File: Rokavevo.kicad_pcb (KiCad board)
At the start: 2 copper layers, 44 parts, among them J1 AudioJack2_Ground_Switch, Q1 BC847, Q2 BC847, Q3 BC847, Q4 BC847, Q5 BC847, SW1 SW_Nidec_CAS-120A1, U1 LM358, Y1 3579kHz

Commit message: Add files via upload
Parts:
- moved L1 2.82 mm to (105.4, 99.3), turned to 180 degrees
- moved C3 1.99 mm to (108.3, 97.7), turned to 90 degrees
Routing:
- net /RF BPF: track 30.3 -> 24.4 mm
- net /ANT: track 10.8 -> 13.6 mm
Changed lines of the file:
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@@
 	(footprint "Capacitor_SMD:C_0805_2012Metric_Pad1.18x1.45mm_HandSolder"
 		(layer "F.Cu")
-		(at 110.2 98.3375 -90)
+		(at 108.3 97.7375 90)
 		(descr "Capacitor SMD 0805 (2012 Metric), square (rectangular) end terminal, IPC-7351 nominal with elongated pad for handsoldering. (Body size source: IPC-SM-782 page 76, https://www.pcb-3d.com/wordpress/wp-content/uploads/ipc-sm-782a_amendment_1_and_2.pdf, https://docs.google.com/spreadsheets/d/1BsfQQcO9C6DZCsRaXUlFlo91Tg2WpOkGARC1WS5S8t0/edit?usp=sharing), generated with kicad-footprint-generator")
 		(tags "capacitor handsolder")
@@
 		(attr smd)
 		(fp_line
-			(start -0.261252 0.735)
-			(end 0.261252 0.735)
+			(start -0.261252 -0.735)
+			(end 0.261252 -0.735)
 			(stroke
 				(width 0.12)
@@
 		)
 		(fp_line
-			(start -0.261252 -0.735)
-			(end 0.261252 -0.735)
+			(start -0.261252 0.735)
+			(end 0.261252 0.735)
 			(stroke
 				(width 0.12)
@@
 		)
 		(fp_line
-			(start -1.88 0.98)
-			(end -1.88 -0.98)
+			(start 1.88 -0.98)
+			(end 1.88 0.98)
 			(stroke
 				(width 0.05)
@@
 		)
 		(fp_line
-			(start 1.88 0.98)
-			(end -1.88 0.98)
+			(start -1.88 -0.98)
+			(end 1.88 -0.98)
 			(stroke
 				(width 0.05)
@@
 		)
 		(fp_line
-			(start -1.88 -0.98)
-			(end 1.88 -0.98)
+			(start 1.88 0.98)
+			(end -1.88 0.98)
 			(stroke
 				(width 0.05)
@@
 		)
 		(fp_line
-			(start 1.88 -0.98)
-			(end 1.88 0.98)
+			(start -1.88 0.98)
+			(end -1.88 -0.98)
 			(stroke
 				(width 0.05)
@@
 		)
 		(fp_line
-			(start -1 0.625)
-			(end -1 -0.625)
+			(start 1 -0.625)
+			(end 1 0.625)
 			(stroke
 				(width 0.1)
@@
 		)
 		(fp_line
-			(start 1 0.625)
-			(end -1 0.625)
+			(start -1 -0.625)
+			(end 1 -0.625)
 			(stroke
 				(width 0.1)
@@
 		)
 		(fp_line
-			(start -1 -0.625)
-			(end 1 -0.625)
+			(start 1 0.625)
+			(end -1 0.625)
 			(stroke
 				(width 0.1)
@@
 		)
 		(fp_line
-			(start 1 -0.625)
-			(end 1 0.625)
+			(start -1 0.625)
+			(end -1 -0.625)
 			(stroke
 				(width 0.1)
@@
 		)
 		(pad "1" smd roundrect
-			(at -1.0375 0 270)
+			(at -1.0375 0 90)
 			(size 1.175 1.45)
 			(layers "F.Cu" "F.Mask" "F.Paste")
@@
 		)
 		(pad "2" smd roundrect
-			(at 1.0375 0 270)
+			(at 1.0375 0 90)
 			(size 1.175 1.45)
 			(layers "F.Cu" "F.Mask" "F.Paste")
@@
 	(footprint "Connector_PinHeader_2.54mm:PinHeader_1x02_P2.54mm_Vertical"
 		(layer "F.Cu")
-		(at 107.2 97.1)
+		(at 105.4 99.275 180)
 		(descr "Through hole straight pin header, 1x02, 2.54mm pitch, single row")
 		(tags "Through hole pin header THT 1x02 2.54mm single row")
@@
 		(attr through_hole)
 		(fp_line
-			(start -1.38 -1.38)
-			(end 0 -1.38)
+			(start 1.38 1.27)
+			(end 1.38 3.92)
 			(stroke
 				(width 0.12)
@@
 		)
 		(fp_line
-			(start -1.38 0)
-			(end -1.38 -1.38)
+			(start -1.38 3.92)
+			(end 1.38 3.92)
 			(stroke
 				(width 0.12)
@@
 		(fp_line
 			(start -1.38 1.27)
-			(end -1.38 3.92)
+			(end 1.38 1.27)
 			(stroke
 				(width 0.12)
@@
 		(fp_line
 			(start -1.38 1.27)
-			(end 1.38 1.27)
+			(end -1.38 3.92)
 			(stroke
 				(width 0.12)
@@
 		)
 		(fp_line
-			(start -1.38 3.92)
-			(end 1.38 3.92)
+			(start -1.38 0)
+			(end -1.38 -1.38)
 			(stroke
 				(width 0.12)
@@
 		)
 		(fp_line
-			(start 1.38 1.27)
-			(end 1.38 3.92)
+			(start -1.38 -1.38)
+			(end 0 -1.38)
 			(stroke
 				(width 0.12)
@@
 		)
 		(fp_line
-			(start -1.77 -1.77)
-			(end -1.77 4.32)
+			(start 1.77 4.32)
+			(end 1.77 -1.77)
 			(stroke
 				(width 0.05)
@@
 		)
 		(fp_line
-			(start -1.77 4.32)
-			(end 1.77 4.32)
+			(start 1.77 -1.77)
+			(end -1.77 -1.77)
 			(stroke
 				(width 0.05)
@@
 		)
 		(fp_line
-			(start 1.77 -1.77)
-			(end -1.77 -1.77)
+			(start -1.77 4.32)
+			(end 1.77 4.32)
 			(stroke
 				(width 0.05)
@@
 		)
 		(fp_line
-			(start 1.77 4.32)
-			(end 1.77 -1.77)
+			(start -1.77 -1.77)
+			(end -1.77 4.32)
 			(stroke
 				(width 0.05)
@@
 		)
 		(fp_line
-			(start -1.27 -0.635)
-			(end -0.635 -1.27)
+			(start 1.27 3.81)
+			(end -1.27 3.81)
 			(stroke
 				(width 0.1)
@@
 		)
 		(fp_line
-			(start -1.27 3.81)
-			(end -1.27 -0.635)
+			(start 1.27 -1.27)
+			(end 1.27 3.81)
 			(stroke
 				(width 0.1)
@@
 		)
 		(fp_line
-			(start 1.27 -1.27)
-			(end 1.27 3.81)
+			(start -1.27 3.81)
+			(end -1.27 -0.635)
 			(stroke
 				(width 0.1)
@@
 		)
 		(fp_line
-			(start 1.27 3.81)
-			(end -1.27 3.81)
+			(start -1.27 -0.635)
+			(end -0.635 -1.27)
 			(stroke
 				(width 0.1)
@@
 		)
 		(pad "1" thru_hole rect
-			(at 0 0)
+			(at 0 0 180)
 			(size 1.7 1.7)
 			(drill 1)
@@
 		)
 		(pad "2" thru_hole circle
-			(at 0 2.54)
+			(at 0 2.54 180)
 			(size 1.7 1.7)
 			(drill 1)
@@
 	)
 	(segment
-		(start 109.935 99.64)
-		(end 110.2 99.375)
+		(start 119.279 94.447644)
+		(end 119.279 92.952356)
 		(width 0.381)
 		(layer "F.Cu")
@@
 	)
 	(segment
-		(start 117.2 98)
-		(end 117.2 96.526644)
-		(width 0.381)
+		(start 108.265 96.735)
+		(end 108.3 96.7)
+		(width 0.2)
 		(layer "F.Cu")
 		(net 3)
 	)
 	(segment
-		(start 108.1 95.5)
-		(end 106.1 95.5)
+		(start 118.326644 92)
+		(end 109.1 92)
 		(width 0.381)
 		(layer "F.Cu")
@@
 	)
 	(segment
-		(start 105.3 96.3)
-		(end 105.3 97.74)
-		(width 0.381)
+		(start 105.4 96.735)
+		(end 108.265 96.735)
+		(width 0.2)
 		(layer "F.Cu")
 		(net 3)
 	)
 	(segment
-		(start 108.9 94.7)
-		(end 108.1 95.5)
+		(start 109.1 92)
+		(end 108.8 92.3)
 		(width 0.381)
 		(layer "F.Cu")
@@
 	)
 	(segment
-		(start 109.960856 92)
-		(end 108.9 93.060856)
+		(start 117.2 98)
+		(end 117.2 96.526644)
 		(width 0.381)
 		(layer "F.Cu")
@@
 	)
 	(segment
-		(start 119.279 92.952356)
-		(end 118.326644 92)
+		(start 117.2 96.526644)
+		(end 119.279 94.447644)
 		(width 0.381)
 		(layer "F.Cu")
@@
 	)
 	(segment
-		(start 106.1 95.5)
-		(end 105.3 96.3)
+		(start 108.3 95.3)
+		(end 108.3 96.7)
 		(width 0.381)
 		(layer "F.Cu")
@@
 	)
 	(segment
-		(start 107.2 99.64)
-		(end 109.935 99.64)
+		(start 108.8 92.3)
+		(end 108.8 94.8)
 		(width 0.381)
 		(layer "F.Cu")
@@
 	)
 	(segment
-		(start 108.9 93.060856)
-		(end 108.9 94.7)
+		(start 119.279 92.952356)
+		(end 118.326644 92)
 		(width 0.381)
 		(layer "F.Cu")
@@
 	)
 	(segment
-		(start 105.3 97.74)
-		(end 107.2 99.64)
+		(start 108.8 94.8)
+		(end 108.3 95.3)
 		(width 0.381)
 		(layer "F.Cu")
@@
 	)
 	(segment
-		(start 118.326644 92)
-		(end 109.960856 92)
+		(start 110.2375 93.6625)
+		(end 110.2 93.7)
 		(width 0.381)
 		(layer "F.Cu")
-		(net 3)
+		(net 4)
 	)
 	(segment
-		(start 117.2 96.526644)
-		(end 119.279 94.447644)
+		(start 112.26 93.84)
+		(end 112 94.1)
 		(width 0.381)
 		(layer "F.Cu")
-		(net 3)
+		(net 4)
 	)
 	(segment
-		(start 119.279 94.447644)
-		(end 119.279 92.952356)
+		(start 108.3 98.775)
+		(end 105.9 98.775)
 		(width 0.381)
 		(layer "F.Cu")
-		(net 3)
+		(net 4)
 	)
 	(segment
-		(start 110.2375 93.6625)
-		(end 110.2 93.7)
+		(start 112 94.1)
+		(end 112 98)
 		(width 0.381)
 		(layer "F.Cu")
@@
 	)
 	(segment
-		(start 111.1 97.1)
-		(end 107.2 97.1)
+		(start 112.26 93.6625)
+		(end 112.26 93.84)
 		(width 0.381)
 		(layer "F.Cu")
@@
 	)
 	(segment
-		(start 110.2 97.3)
-		(end 110.2 93.7)
+		(start 112 98)
+		(end 111.225 98.775)
 		(width 0.381)
 		(layer "F.Cu")
@@
 	)
 	(segment
-		(start 112 98)
-		(end 111.1 97.1)
+		(start 105.9 98.775)
+		(end 105.4 99.275)
+		(width 0.381)
+		(layer "F.Cu")
+		(net 4)
+	)
+	(segment
+		(start 111.225 98.775)
+		(end 108.3 98.775)
 		(width 0.381)
 		(layer "F.Cu")
@@
 		(polygon
 			(pts
-				(xy 100 73) (xy 163.3 73) (xy 163.404418 129.389582) (xy 100 129) (xy 100 73) (xy 100 73)
+				(xy 100 73) (xy 163.3 73) (xy 163.404418 129.389582) (xy 100 129)
 			)
 		)

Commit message: Add files via upload
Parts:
- moved J1 10.3 mm to (157.2, 86.2)
- moved C13 10.2 mm to (143.3, 82.8)
- moved D3 8.51 mm to (110.5, 123.2)
- moved D4 8.51 mm to (115.5, 123.2)
- moved R8 8.19 mm to (115.5, 116.7), turned to -90 degrees
- moved RV1 6.76 mm to (148.9, 111.4)
- moved R11 5.90 mm to (134.7, 120.2)
- moved C8 5.68 mm to (134.1, 117.0)
- moved Q4 5.24 mm to (121.0, 101.0)
- moved C6 5.03 mm to (128.0, 99.8)
- moved Q5 4.61 mm to (128.7, 105.6)
- moved C11 4.39 mm to (135.0, 103.2)
- moved C9 4.39 mm to (123.5, 113.2)
- moved R10 4.39 mm to (137.5, 94.2)
- moved R12 4.39 mm to (117.7, 109.2)
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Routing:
- net Net-(U1B--): track 9.46 -> 23.5 mm
- net Net-(D5-K): track 68.6 -> 75.9 mm
- net /ANT: track 13.6 -> 19.6 mm
- net /RF BPF: track 24.4 -> 30.4 mm
- net Net-(U1B-+): track 11.3 -> 15.3 mm
- net /LNA: track 6.41 -> 10.4 mm
- net Net-(D2-K): track 4.00 -> 7.04 mm
- net Net-(U1A--): track 6.98 -> 9.77 mm
- net Net-(C12-Pad1): track 8.09 -> 5.54 mm
- net Net-(Q3-E): track 8.02 -> 10.6 mm
- net Net-(Q3-B): track 21.5 -> 19.6 mm
- net Net-(Q2-E): track 10.4 -> 12.3 mm
- net /SBM: track 29.7 -> 31.3 mm

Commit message: Add files via upload
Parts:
- removed J1: AudioJack2_Ground_Switch, Connector_Audio:Jack_3.5mm_CUI_SJ1-3515N_Horizontal
- added J2: AudioJack3_SwitchTR, Connector_Audio:Jack_3.5mm_CUI_SJ1-3515N_Horizontal, B.Cu at (157.3, 87.8)
- BT1, L1, RV1, SW1, Y1: moved to B.Cu
- moved C13 13.9 mm to (148.4, 95.8)
- moved RV1 9.90 mm to (139.0, 111.4)
- moved L1 1.41 mm to (105.0, 99.8), turned to 0 degrees
- turned BT1 to 180 degrees
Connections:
- RV1 pad 1: Net-(U1B-+) -> Net-(C12-Pad1)
- RV1 pad 3: Net-(C12-Pad1) -> Net-(U1B-+)
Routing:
- net Net-(U1B--): track 23.5 -> 8.92 mm
- net Net-(D5-K): track 75.9 -> 77.8 mm
- net /RF BPF: track 30.4 -> 28.9 mm
- net /ANT: track 19.6 -> 18.1 mm
- net Net-(Q2-B): track 37.4 -> 36.4 mm
- net /SBM: track 31.3 -> 32.1 mm
- net Net-(C13-Pad2): track 23.0 -> 23.6 mm
- removed copper zone on B.Cu, net GND

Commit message: Add files via upload
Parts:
- RV1: footprint Connector_PinHeader_2.54mm:PinHeader_1x03_P2.54mm_Vertical -> Potentiometer_THT:Potentiometer_Omeg_PC16BU_Vertical
- moved BT1 48.3 mm to (151.5, 74.5), turned to 90 degrees
- moved J2 42.2 mm to (144.8, 128.1), turned to 90 degrees
- moved D3 41.9 mm to (109.4, 81.3), turned to 90 degrees
- moved D2 39.5 mm to (116.3, 77.8), turned to 0 degrees
- moved C2 37.5 mm to (141.0, 77.2), turned to 0 degrees
- moved D4 37.4 mm to (109.4, 86.3), turned to 90 degrees
- moved SW1 37.4 mm to (150.1, 83.5), turned to 0 degrees
- moved L1 36.7 mm to (132.8, 75.8), turned to -90 degrees
- moved D1 36.1 mm to (121.8, 77.8), turned to 0 degrees
- moved R6 35.1 mm to (126.6, 77.2), turned to 180 degrees
- moved C1 33.6 mm to (141.0, 80.2), turned to 0 degrees
- moved Y1 32.3 mm to (109.5, 93.7), turned to 0 degrees
- moved D5 30.7 mm to (151.6, 95.2), turned to 90 degrees
- moved R7 30.5 mm to (121.0, 82.5), turned to -90 degrees
- moved R8 30.3 mm to (115.9, 86.3), turned to 180 degrees
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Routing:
- net Net-(U1A--): track 9.77 -> 14.1 mm
- net Net-(U1B-+): track 15.3 -> 19.0 mm
- net /LNA: track 10.4 -> 13.8 mm
- net Net-(C12-Pad1): track 5.54 -> 3.04 mm
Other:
- board text added: "Rókavevő 80m Gaben 2025 Prototype I."
- board text removed: "Rókavevő 80m Gaben 2025 Prototipus I."

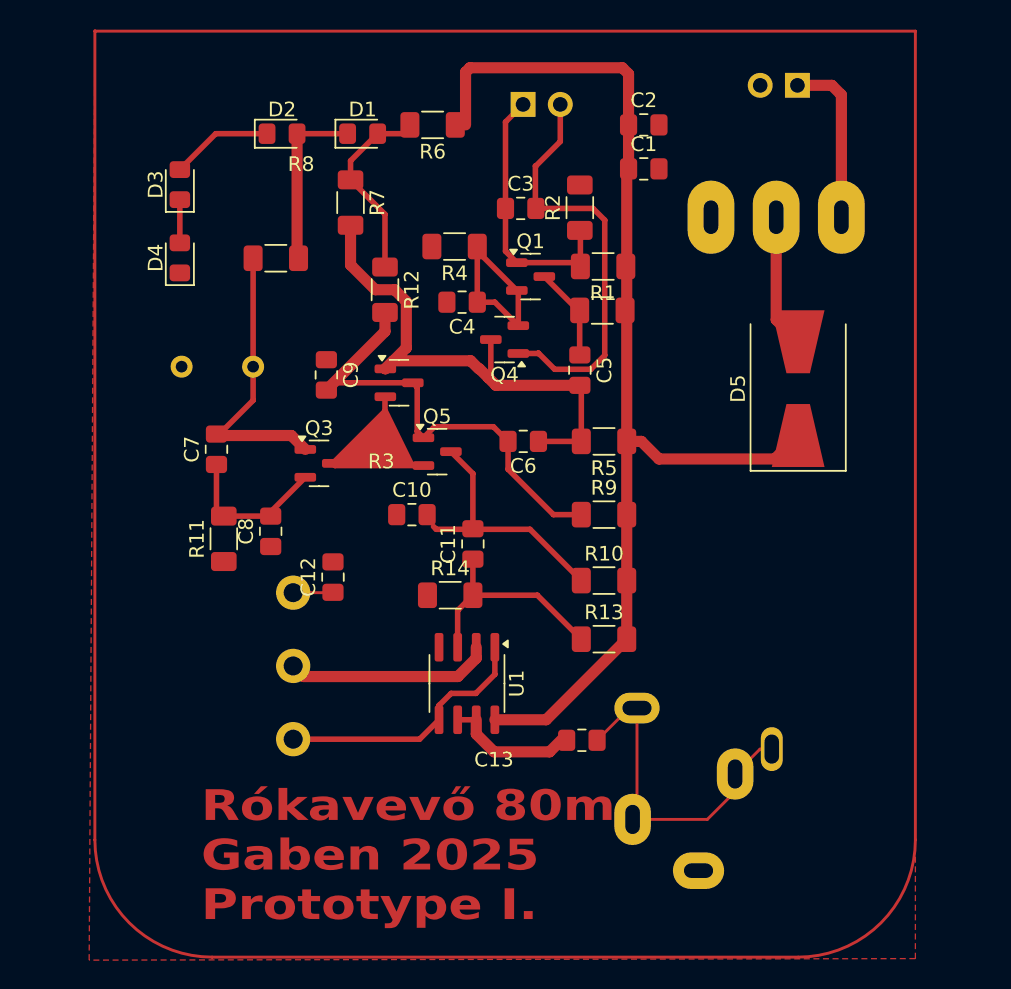
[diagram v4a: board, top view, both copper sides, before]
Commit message: Prototype II
Fixed schematic, new pcb design, Printable mask
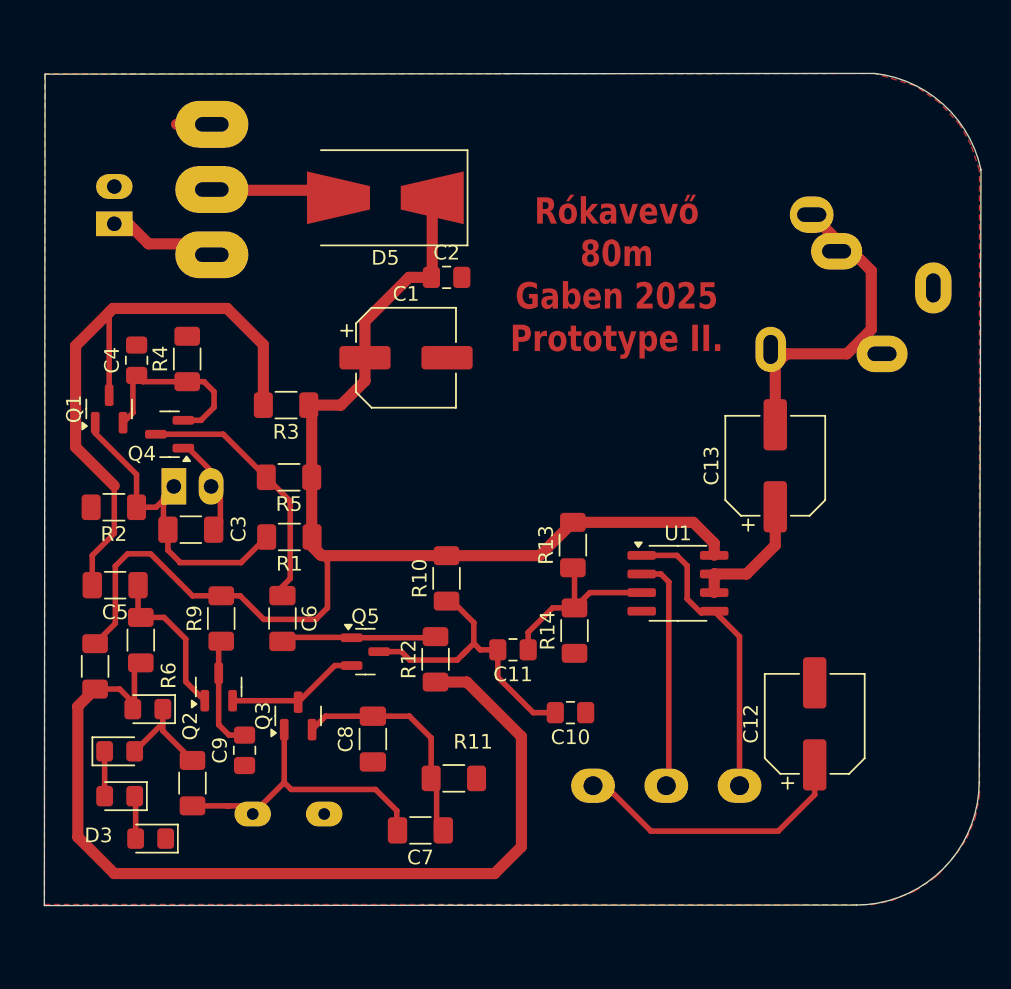
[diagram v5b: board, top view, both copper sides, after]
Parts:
- C1, C12, C13: footprint Capacitor_SMD:C_0805_2012Metric_Pad1.18x1.45mm_HandSolder -> Capacitor_SMD:CP_Elec_6.3x5.3
- C3: footprint Capacitor_SMD:C_0805_2012Metric_Pad1.18x1.45mm_HandSolder -> Capacitor_SMD:C_1206_3216Metric_Pad1.33x1.80mm_HandSolder
- C5, C6, C7, C8: value 223 -> 181; footprint Capacitor_SMD:C_0805_2012Metric_Pad1.18x1.45mm_HandSolder -> Capacitor_SMD:C_1206_3216Metric_Pad1.33x1.80mm_HandSolder
- moved BT1 47.6 mm to (104.9, 84.0), turned to 0 degrees
- moved D2 43.6 mm to (105.3, 120.0)
- moved R6 43.5 mm to (103.6, 114.2), turned to -90 degrees
- moved J2 42.9 mm to (160.8, 88.3), turned to 180 degrees
- moved D3 41.9 mm to (105.3, 123.0), turned to 180 degrees
- moved D1 41.9 mm to (107.2, 117.1), turned to 180 degrees
- moved D4 39.7 mm to (107.4, 125.9), turned to 180 degrees
- moved SW1 38.6 mm to (111.6, 81.6), turned to -90 degrees
- moved R2 37.8 mm to (104.9, 103.3), turned to 180 degrees
- moved R8 36.3 mm to (110.2, 122.2), turned to -90 degrees
- moved L1 35.3 mm to (109.0, 101.9)
- moved C5 34.9 mm to (105.0, 108.6), turned to 180 degrees
- moved C12 34.4 mm to (152.7, 118.1)
- moved R7 33.1 mm to (106.7, 112.4), turned to 90 degrees
- moved Y1 32.0 mm to (119.2, 124.3), turned to 180 degrees
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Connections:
- C5 pad 1: Net-(Q1-C) -> Net-(Q2-B)
- C5 pad 2: Net-(Q2-B) -> Net-(Q1-C)
- C6 pad 1: Net-(Q2-B) -> Net-(Q4-C)
- C9 pad 2: /SBM -> Net-(Q2-C)
- Q2 pad 3: /SBM -> Net-(Q2-C)
- Q4 pad 3: Net-(Q2-B) -> Net-(Q4-C)
- R5 pad 2: Net-(Q2-B) -> Net-(Q4-C)
- R9 pad 1: /SBM -> Net-(Q2-C)
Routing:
- net Net-(D1-A): track 13.1 -> 64.4 mm
- net Net-(Q1-C): track 6.41 -> 42.7 mm
- net Net-(Q2-B): track 36.4 -> 10.7 mm
- net /RF BPF: track 28.9 -> 7.00 mm
- net /SBM: track 32.1 -> 10.6 mm
- net Net-(Q4-C): track 0.00 -> 18.0 mm
- net Net-(C12-Pad1): track 3.04 -> 18.6 mm
- net Net-(D5-K): track 77.8 -> 87.4 mm
- net Net-(Q2-C): track 0.00 -> 8.47 mm
- net Net-(BT1-+): track 11.6 -> 4.99 mm
- net Net-(Q3-E): track 10.6 -> 15.9 mm
- net Net-(D1-K): track 12.0 -> 7.52 mm
- net Net-(D2-K): track 7.04 -> 3.06 mm
- net Net-(C13-Pad2): track 23.6 -> 19.9 mm
- net /ANT: track 18.1 -> 21.7 mm
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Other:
- board outline added: 63.9 x 56.8 mm
- board text added: "Rókavevő 80m Gaben 2025 Prototype II."
- board text removed: "Rókavevő 80m Gaben 2025 Prototype I."
